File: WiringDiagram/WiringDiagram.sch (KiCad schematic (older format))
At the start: 8 parts, among them J1&? SafetyLights

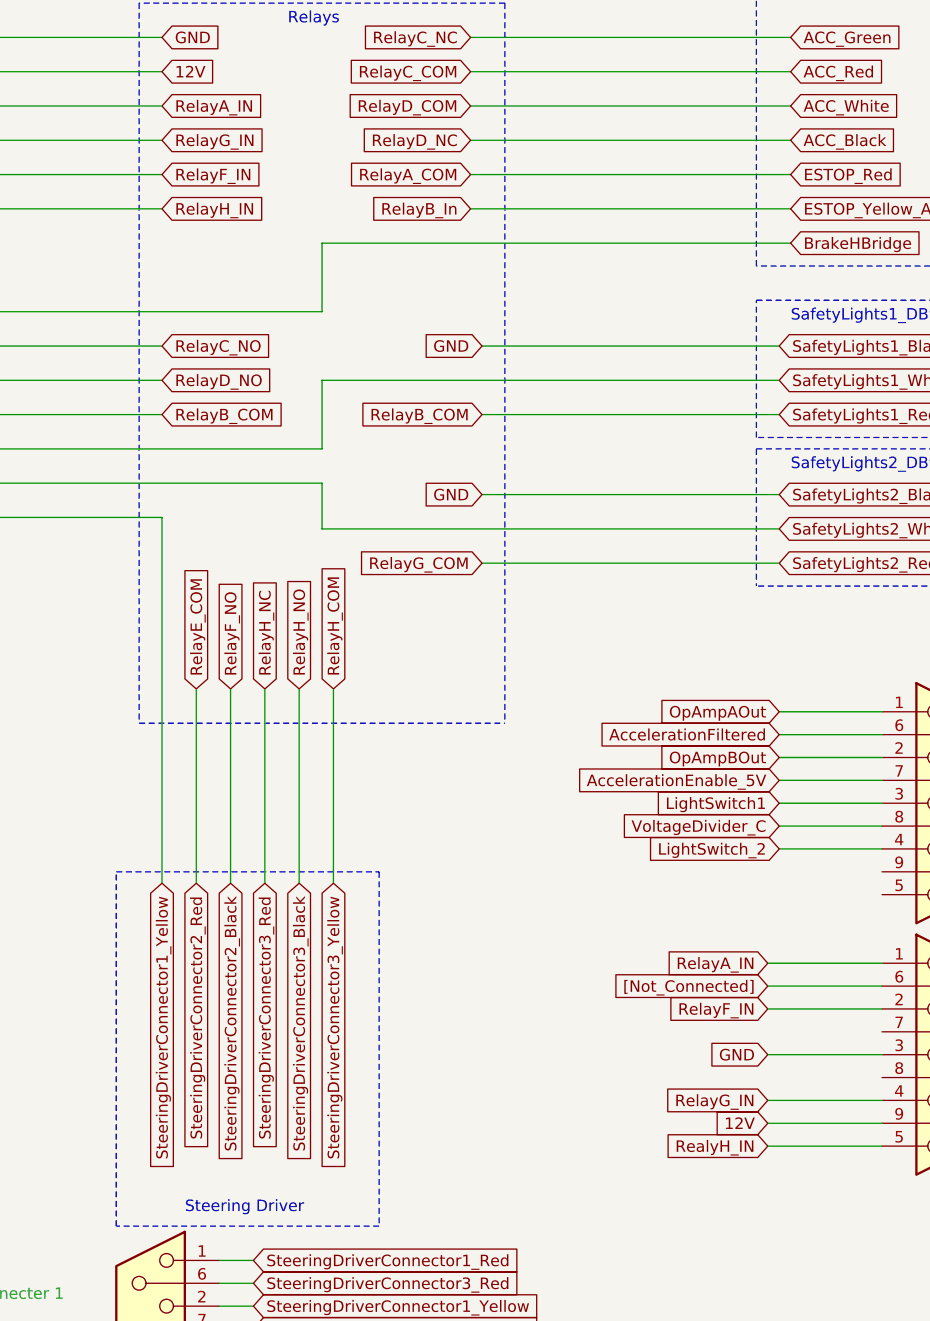
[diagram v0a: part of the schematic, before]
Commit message: inverted RelaysIN F & H Label in 'Wiring Diagram' and Relay Connector 2  and cleaned ECU Prototype Schematic
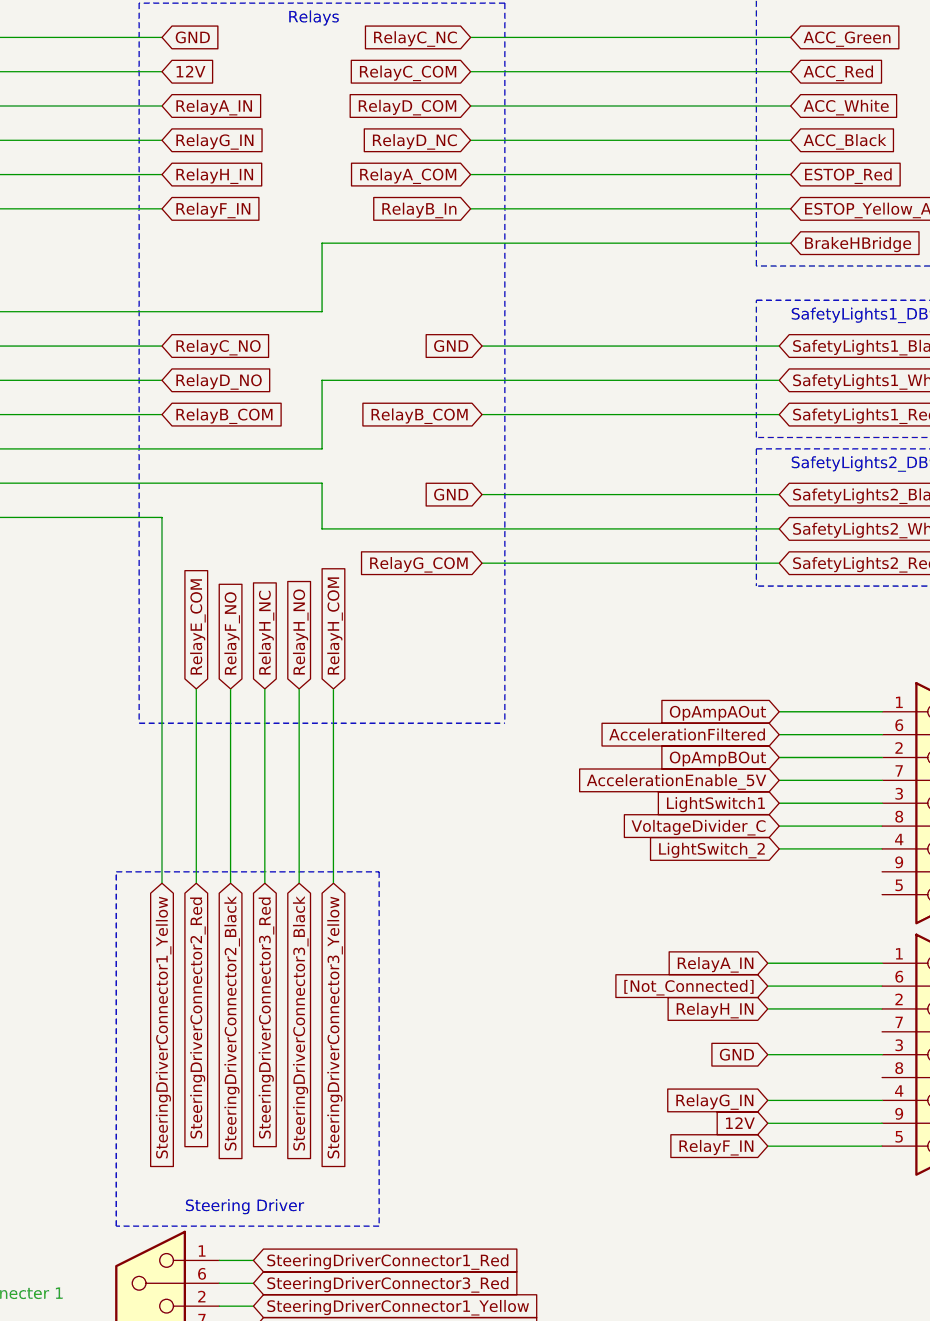
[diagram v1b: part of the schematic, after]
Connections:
- net labels removed: RealyH_IN
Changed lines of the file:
@@
 RelayB_COM
 Text GLabel 8300 2150 2    50   Input ~ 0
+RelayH_IN
+Text GLabel 8300 2300 2    50   Input ~ 0
 RelayF_IN
-Text GLabel 8300 2300 2    50   Input ~ 0
-RelayH_IN
 Wire Wire Line
 	6300 2150 8300 2150
@@
 $EndComp
 Text GLabel 10950 6400 0    50   Input ~ 0
-RealyH_IN
+RelayF_IN
 $Comp
 L Connector:DB9_Female J?
@@
 GND
 Text GLabel 10950 5800 0    50   Input ~ 0
-RelayF_IN
+RelayH_IN
 Text GLabel 10950 5600 0    50   Input ~ 0
 RelayA_IN

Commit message: Cleaned Up Diagram, Added I/O Spreadsheet for Diagnostics and Validation
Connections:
- no-connect marks 0 -> 15
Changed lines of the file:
@@
 L power:GND #PWR?
 U 1 1 5E1E89BD
-P 6750 1450
-F 0 "#PWR?" H 6750 1200 50  0001 C CNN
-F 1 "GND" H 6755 1277 50  0000 C CNN
-F 2 "" H 6750 1450 50  0001 C CNN
-F 3 "" H 6750 1450 50  0001 C CNN
-	1    6750 1450
+P 6500 1450
+F 0 "#PWR?" H 6500 1200 50  0001 C CNN
+F 1 "GND" H 6505 1277 50  0000 C CNN
+F 2 "" H 6500 1450 50  0001 C CNN
+F 3 "" H 6500 1450 50  0001 C CNN
+	1    6500 1450
 	1    0    0    -1
 $EndComp
 Text GLabel 6150 1450 3    50   Input ~ 0
+12V
+Text GLabel 6700 1450 3    50   Input ~ 0
 5V
-Text GLabel 6550 1450 3    50   Input ~ 0
-12V
 Wire Wire Line
 	6150 1450 6150 800
@@
 	6350 1450 6350 800
 Wire Wire Line
-	6550 1450 6550 800
-Wire Wire Line
-	6750 1450 6750 800
+	6700 1450 6700 800
+Wire Wire Line
+	6500 1450 6500 800
 Text Notes 6050 700  0    50   ~ 0
 To Power Distribution
@@
 Text GLabel 6600 7300 0    50   Input ~ 0
 5v
+NoConn ~ 1650 3800
+NoConn ~ 1650 4000
+NoConn ~ 11450 5200
+NoConn ~ 11450 5300
+NoConn ~ 11450 5900
+NoConn ~ 11450 6100
+NoConn ~ 8550 7600
+NoConn ~ 12450 3050
+NoConn ~ 12450 3150
+NoConn ~ 12450 3250
+NoConn ~ 12450 3450
+NoConn ~ 12450 3550
+NoConn ~ 12450 3750
+NoConn ~ 13150 2000
+NoConn ~ 13150 2200
 $EndSCHEMATC
